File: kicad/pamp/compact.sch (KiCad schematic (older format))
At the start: 92 parts, among them J1 input, J2 output, J3 power, J4 Conn_01x02, Q1 BC560C, Q10 MJE340, Q11 BC546B, Q12 BC556B, Q13 2SC4793, Q14 Q_PNP_BCE, Q15 MJL3281, Q16 MJL1302, Q17 BC546B, Q18 BC546B, Q2 BC550C, Q3 2SA1381F, Q4 BC550C, Q5 BC560C, Q6 BC546B, Q7 BC546B, Q8 2SC3503F, Q9 2SA1381F

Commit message: First prerelease.
Signed-off-by: Nenad Radulovic <nenad.b.radulovic@gmail.com>
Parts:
- removed Q11: BC546B, Package_TO_SOT_THT:TO-92L_Inline, symbol Device:Q_NPN_CBE
- removed Q12: BC556B, Package_TO_SOT_THT:TO-92L_Inline, symbol Device:Q_PNP_CBE
- removed R16, R17: 330, Resistor_THT:R_Axial_DIN0207_L6.3mm_D2.5mm_P10.16mm_Horizontal, symbol Device:R
- removed R18, R19: 750, Resistor_THT:R_Axial_DIN0207_L6.3mm_D2.5mm_P10.16mm_Horizontal, symbol Device:R
- removed R39, R40: 27k, Resistor_THT:R_Axial_DIN0207_L6.3mm_D2.5mm_P10.16mm_Horizontal, symbol Device:R
- added D6, D7: BAV21, Diode_THT:D_DO-41_SOD81_P7.62mm_Horizontal, symbol Device:D
- added LOGO1: Logo_Open_Hardware_Small, Symbol:KiCad-Logo_5mm_Copper, symbol Graphic:Logo_Open_Hardware_Small
- Q1, Q2, Q4, Q5, Q6, Q7: footprint Package_TO_SOT_THT:TO-92L_Inline -> Package_TO_SOT_THT:TO-92L_Inline_Wide
- Q11: renamed from Q17; footprint Package_TO_SOT_THT:TO-92L_Inline -> Package_TO_SOT_THT:TO-92L_Inline_Wide
- Q12: renamed from Q18; footprint Package_TO_SOT_THT:TO-92L_Inline -> Package_TO_SOT_THT:TO-92L_Inline_Wide
- renumbered C15 to C1, C7 to C10, C8 to C11, C9 to C12, C10 to C13, C11 to C14, C12 to C15, C13 to C16, C16 to C2, C1 to C3, C2 to C4, C14 to C5, C3 to C6, C4 to C7, C5 to C8, C6 to C9, D8 to D10, D6 to D8, D7 to D9, J4 to J1, J1 to J2, J2 to J3, J3 to J4, R9 to R10, R35 to R11, R36 to R12, R37 to R13, R10 to R14, R11 to R15, R12 to R16, R13 to R17, R38 to R18, R14 to R19, R15 to R20, R20 to R21, R21 to R22, R22 to R23, R23 to R24, R24 to R25, R25 to R26, R26 to R27, R27 to R28, R28 to R29, R29 to R30, R30 to R31, R31 to R32, R32 to R33, R33 to R34, R34 to R7, R7 to R8, R8 to R9
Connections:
- net at C8.1, D10.1 (K), D9.2 (A)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: now also D6.2 (A), D7.1 (K)
- net at D5.1 (K): now also C6.1, Q10.2 (C), R17.2, R19.1
- net at C5.1, C6.2, D4.1 (K)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: now also D8.2 (A); no longer D8.1 (K)
- new net: D5.2 (A), D6.1 (K)
- new net: D7.2 (A), D8.1 (K)
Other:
- moved on the sheet: D5, D8

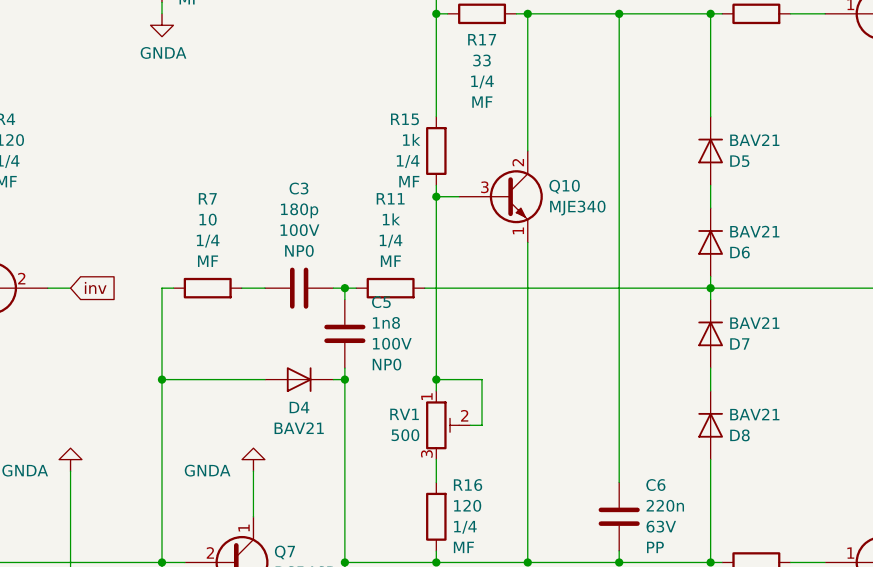
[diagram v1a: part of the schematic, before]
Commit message: Made the compensation scheme much simpler.
Signed-off-by: Nenad Radulovic <nenad.b.radulovic@gmail.com>
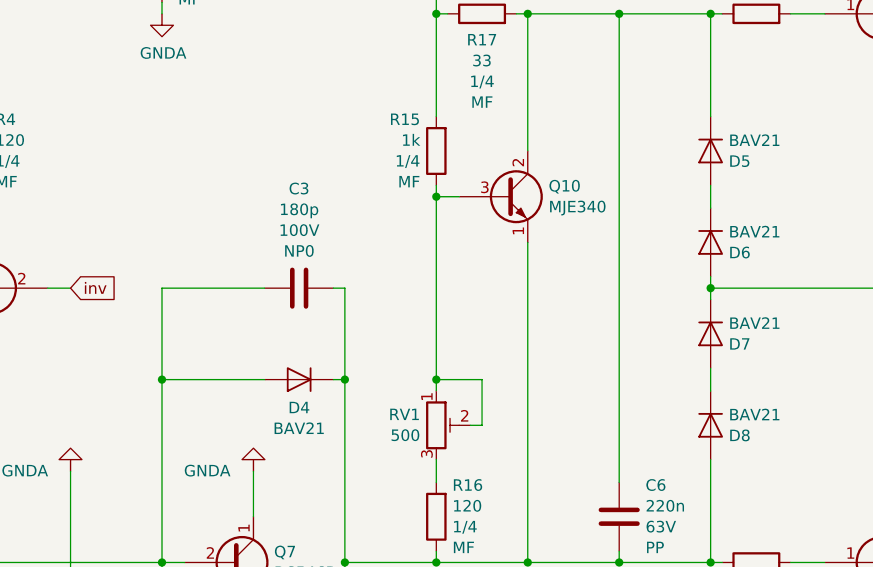
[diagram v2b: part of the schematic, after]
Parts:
- removed C5: 1n8, Capacitor_THT:C_Disc_D8.0mm_W2.5mm_P5.00mm, symbol Device:C
- removed R11: 1k, Resistor_THT:R_Axial_DIN0207_L6.3mm_D2.5mm_P10.16mm_Horizontal, symbol Device:R
- removed R7: 10, Resistor_THT:R_Axial_DIN0207_L6.3mm_D2.5mm_P10.16mm_Horizontal, symbol Device:R
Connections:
- net at C6.2, D4.1 (K), D8.2 (A)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: now also C3.1
- net at D4.2 (A), Q1.1 (C), Q2.1 (C)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: now also C3.2
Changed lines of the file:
@@
 EESchema Schematic File Version 4
-LIBS:compact-cache
-EELAYER 26 0
+EELAYER 30 0
 EELAYER END
 $Descr A4 11693 8268
@@
 $EndComp
 Wire Wire Line
-	3050 3600 3150 3600
-Wire Wire Line
 	2700 3600 2700 4000
 $Comp
@@
 Wire Wire Line
 	1100 5800 1100 6000
-Wire Wire Line
-	3500 3600 3500 3650
-Wire Wire Line
-	2700 3600 2750 3600
 Wire Wire Line
 	9200 3700 9300 3700
@@
 	-1   0    0    1
 $EndComp
-$Comp
-L Device:C C5
-U 1 1 5D3942BD
-P 3500 3800
-F 0 "C5" H 3385 3663 50  0000 R CNN
-F 1 "1n8" H 3385 3754 50  0000 R CNN
-F 2 "Capacitor_THT:C_Disc_D8.0mm_W2.5mm_P5.00mm" H 3538 3650 50  0001 C CNN
-F 3 "~" H 3500 3800 50  0001 C CNN
-F 4 "100V" H 3385 3845 50  0000 R CNN "Voltage"
-F 5 "NP0" H 3385 3936 50  0000 R CNN "Type"
-	1    3500 3800
-	-1   0    0    1
-$EndComp
 Wire Wire Line
 	3450 3600 3500 3600
-Wire Wire Line
-	3500 3600 3550 3600
-Connection ~ 3500 3600
-Wire Wire Line
-	3500 3950 3500 4000
-$Comp
-L Device:R R7
-U 1 1 5D3ADEF7
-P 2900 3600
-F 0 "R7" V 3289 3600 50  0000 C CNN
-F 1 "10" V 3198 3600 50  0000 C CNN
-F 2 "Resistor_THT:R_Axial_DIN0207_L6.3mm_D2.5mm_P10.16mm_Horizontal" V 2830 3600 50  0001 C CNN
-F 3 "http://www.farnell.com/datasheets/1716726.pdf" H 2900 3600 50  0001 C CNN
-F 4 "1/4" V 3107 3600 50  0000 C CNN "Power"
-F 5 "MF" V 3016 3600 50  0000 C CNN "Type"
-F 6 "Multicomp: MF25 120R" H 2900 3600 50  0001 C CNN "Manufacturer1"
-F 7 "Farnell: " H 2900 3600 50  0001 C CNN "Supplier1A:"
-	1    2900 3600
-	0    -1   -1   0
-$EndComp
-$Comp
-L Device:R R11
-U 1 1 5D3AEE03
-P 3700 3600
-F 0 "R11" V 4089 3600 50  0000 C CNN
-F 1 "1k" V 3998 3600 50  0000 C CNN
-F 2 "Resistor_THT:R_Axial_DIN0207_L6.3mm_D2.5mm_P10.16mm_Horizontal" V 3630 3600 50  0001 C CNN
-F 3 "http://www.farnell.com/datasheets/1716726.pdf" H 3700 3600 50  0001 C CNN
-F 4 "1/4" V 3907 3600 50  0000 C CNN "Power"
-F 5 "MF" V 3816 3600 50  0000 C CNN "Type"
-F 6 "Multicomp: MF25 1k" H 3700 3600 50  0001 C CNN "Manufacturer1"
-F 7 "Farnell: 9341102" H 3700 3600 50  0001 C CNN "Supplier1A:"
-	1    3700 3600
-	0    -1   -1   0
-$EndComp
-Wire Wire Line
-	3850 3600 5100 3600
 $Comp
 L Device:C C1
@@
 Wire Wire Line
 	5100 3550 5100 3600
+Wire Wire Line
+	3500 3600 3500 4000
+Wire Wire Line
+	2700 3600 3150 3600
 $EndSCHEMATC

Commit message: feat: project organization
Signed-off-by: Nenad Radulovic <nenad.b.radulovic@gmail.com>
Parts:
- removed C1, C2: 220p, Capacitor_THT:C_Disc_D8.0mm_W2.5mm_P5.00mm, symbol Device:C
- removed C13: 100u, Capacitor_THT:CP_Radial_D10.0mm_P3.50mm, symbol Device:CP
- removed C8: 8.2p, Capacitor_THT:C_Disc_D3.0mm_W2.0mm_P2.50mm, symbol Device:C
- removed D3, D4, D5, D8: BAV21, Diode_THT:D_DO-41_SOD81_P7.62mm_Horizontal, symbol Device:D
- removed J1: Conn_01x02, Connector_PinHeader_2.54mm:PinHeader_1x02_P2.54mm_Vertical, symbol Connector_Generic:Conn_01x02
- removed Q11, Q12, Q7: BC546B, Package_TO_SOT_THT:TO-92L_Inline_Wide, symbol Device:Q_NPN_CBE
- removed Q2, Q4: BC550C, Package_TO_SOT_THT:TO-92L_Inline_Wide, symbol Device:Q_NPN_CBE
- removed R13, R18: 10k, Resistor_THT:R_Axial_DIN0207_L6.3mm_D2.5mm_P10.16mm_Horizontal, symbol Device:R
- removed R5: 100, Resistor_THT:R_Axial_DIN0207_L6.3mm_D2.5mm_P10.16mm_Horizontal, symbol Device:R
- removed R8: 910, Resistor_THT:R_Axial_DIN0207_L6.3mm_D2.5mm_P10.16mm_Horizontal, symbol Device:R
- added C10: 100u, Capacitor_THT:CP_Radial_D8.0mm_P2.50mm, symbol Device:CP
- added C4: 470u, Capacitor_THT:CP_Radial_D10.0mm_P3.50mm, symbol Device:CP
- added Q8: 2SA1381F, Package_TO_SOT_THT:TO-126-3_Horizontal_TabDown, symbol Device:Q_PNP_ECB
- added R17: 20, Resistor_THT:R_Axial_DIN0207_L6.3mm_D2.5mm_P10.16mm_Horizontal, symbol Device:R
- added R6: 4k7, Resistor_THT:R_Axial_DIN0411_L9.9mm_D3.6mm_P12.70mm_Horizontal, symbol Device:R
- added R7: 680, Resistor_THT:R_Axial_DIN0207_L6.3mm_D2.5mm_P10.16mm_Horizontal, symbol Device:R
- C2: renamed from C3; value 180p -> 100p
- Q5: renamed from Q9; footprint Package_TO_SOT_THT:TO-126-3_Horizontal_TabDown -> Package_TO_SOT_THT:TO-126-3_Vertical
- Q6: renamed from Q8; footprint Package_TO_SOT_THT:TO-126-3_Horizontal_TabDown -> Package_TO_SOT_THT:TO-126-3_Vertical
- R1, R4: value 120 -> 200
- R10: renamed from R15; value 1k -> 680
- R11: renamed from R16; value 120 -> 240
- R12: value 10k -> 150; Manufacturer1 Multicomp: MF25 10K -> Multicomp: MF25 330R; Supplier1A: Farnell: 9341110 -> Farnell: 9341730
- R13: renamed from R10; value 24 -> 20
- R14: renamed from R17; value 33 -> 20
- R2: value 100 -> 300
- R3: value 330 -> 150
- R8: renamed from R9; value 330 -> 300
- R9: renamed from R14; value 100 -> 39
- renumbered C4 to C1, C14 to C11, C15 to C12, C16 to C13, C6 to C3, C7 to C5, C9 to C6, C10 to C7, C11 to C8, C12 to C9, D6 to D3, D7 to D4, D9 to D5, D10 to D6, J2 to J1, J3 to J2, J4 to J3, Q14 to Q10, Q15 to Q11, Q16 to Q12, Q3 to Q2, Q5 to Q3, Q6 to Q4, Q10 to Q7, Q13 to Q9, R19 to R15, R20 to R16, R21 to R18, R22 to R19, R23 to R20, R24 to R21, R25 to R22, R26 to R23, R27 to R24, R28 to R25, R29 to R26, R30 to R27, R31 to R28, R32 to R29, R33 to R30, R34 to R31, R6 to R5
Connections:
- net GNDA: now also C4.1, R6.1; no longer R5.1
- net VSS: now also R17.2; no longer Q4.3 (E), R13.2, R2.1
- net at C3.1, Q7.2 (C), R14.2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: now also D3.1 (K)
- net at D4.2 (A): now also C2.1, C3.2, Q7.1 (E), R11.1, R12.2, R16.1, Q8.1 (E)
- net at Q6.1 (E), R13.1: now also Q3.1 (C), R2.1, Q8.2 (C), R7.2; no longer Q4.2 (B)
- net at R12.1: now also Q6.2 (C), Q8.3 (B); no longer Q6.3 (B)
- net at C2.2, Q1.1 (C), Q4.1 (C): now also Q6.3 (B), R2.2
- net at Q5.3 (B), R8.2: no longer C1.2
- net at Q2.3 (B), R5.2, R8.1: now also D2.1 (K)
- net at R29.1: now also C10.1
- net at J1.3 (Pin_3), R28.2: now also C10.2
- new net: Q4.2 (B), R7.1
- new net: C4.2, Q4.3 (E), R13.2, R17.1
- new net: C1.2, R5.1, R6.2
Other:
- moved on the sheet: C2, D1, D2, Q4, Q6, R13, R2
